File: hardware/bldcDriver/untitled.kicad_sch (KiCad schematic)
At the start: 84 parts, among them Q1 KNY3406C, Q10 KNY3406C, Q11 KNY3406C, Q12 KNY3406C, Q2 KNY3406C, Q3 KNY3406C, Q4 KNY3406C, Q5 KNY3406C, Q6 KNY3406C, Q7 KNY3406C, Q8 KNY3406C, Q9 KNY3406C, U1 FD6288Q, U4 FD6288Q

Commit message: motor sch update
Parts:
- renumbered C33 to C22, C34 to C23, C35 to C24, C31 to C25, C36 to C26, C32 to C27, C37 to C28, C23 to C29, C24 to C30, C38 to C31, C39 to C32, C22 to C33, C40 to C34, C25 to C35, C26 to C36, C41 to C37, C42 to C38, C27 to C39, C43 to C40, C28 to C41, C44 to C43, C30 to C45, Q2 to Q1, Q6 to Q10, Q1 to Q2, Q7 to Q3, Q8 to Q4, Q3 to Q5, Q4 to Q6, Q9 to Q7, Q10 to Q8, Q5 to Q9, R29 to R10, R12 to R11, R30 to R12, R8 to R13, R9 to R14, R31 to R15, R32 to R16, R7 to R17, R10 to R18, R33 to R19, R34 to R20, R14 to R21, R15 to R22, R35 to R23, R36 to R24, R16 to R25, R37 to R26, R17 to R27, R18 to R28, R38 to R29, R39 to R30, R19 to R31, R20 to R32, R40 to R33, R41 to R34, R24 to R41, R25 to R42, R45 to R43, R46 to R44, R26 to R45, R27 to R46, R11 to R7, R13 to R8, R28 to R9

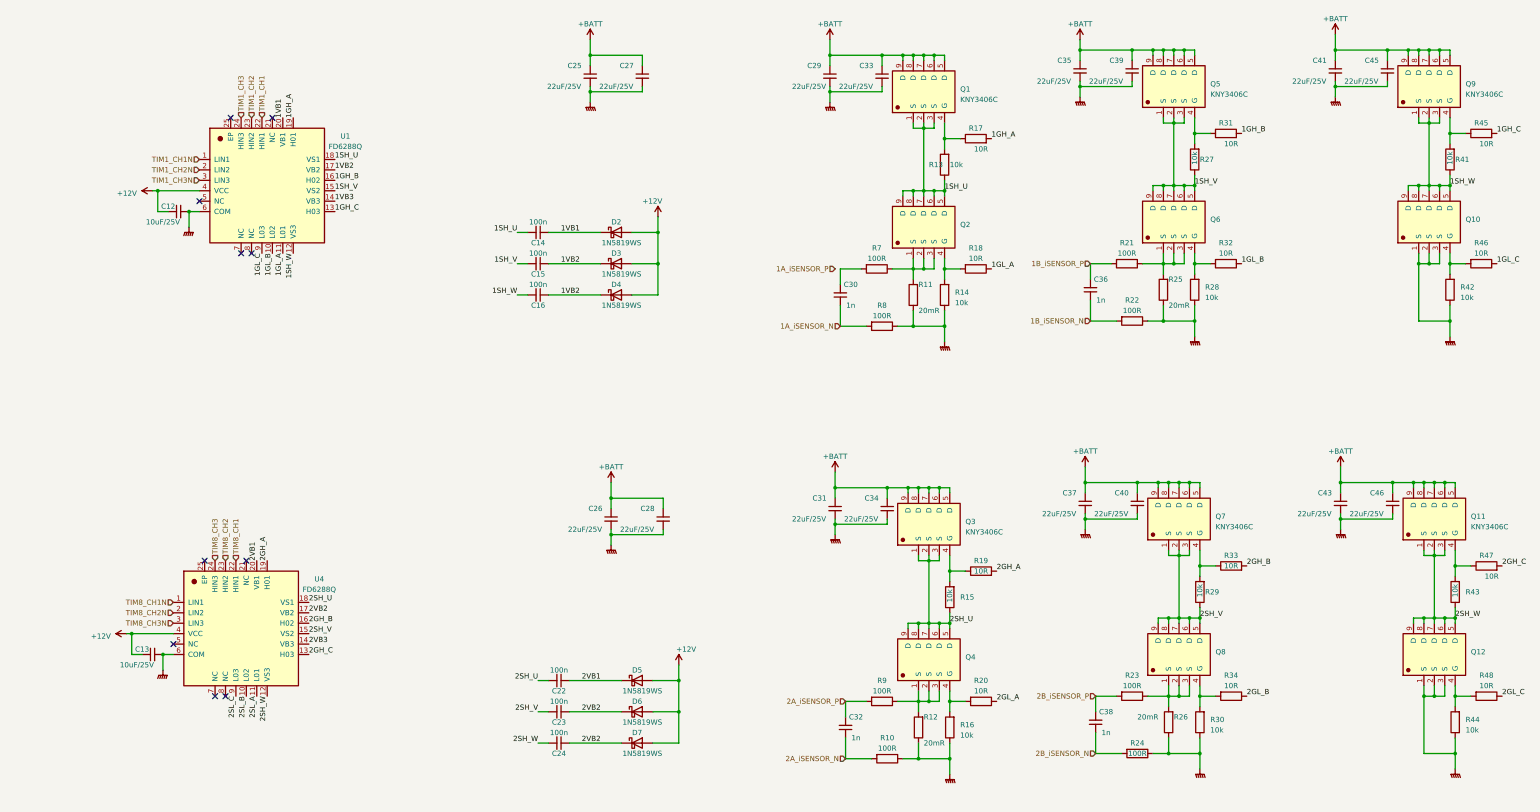
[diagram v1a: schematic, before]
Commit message: motorDriver sch update
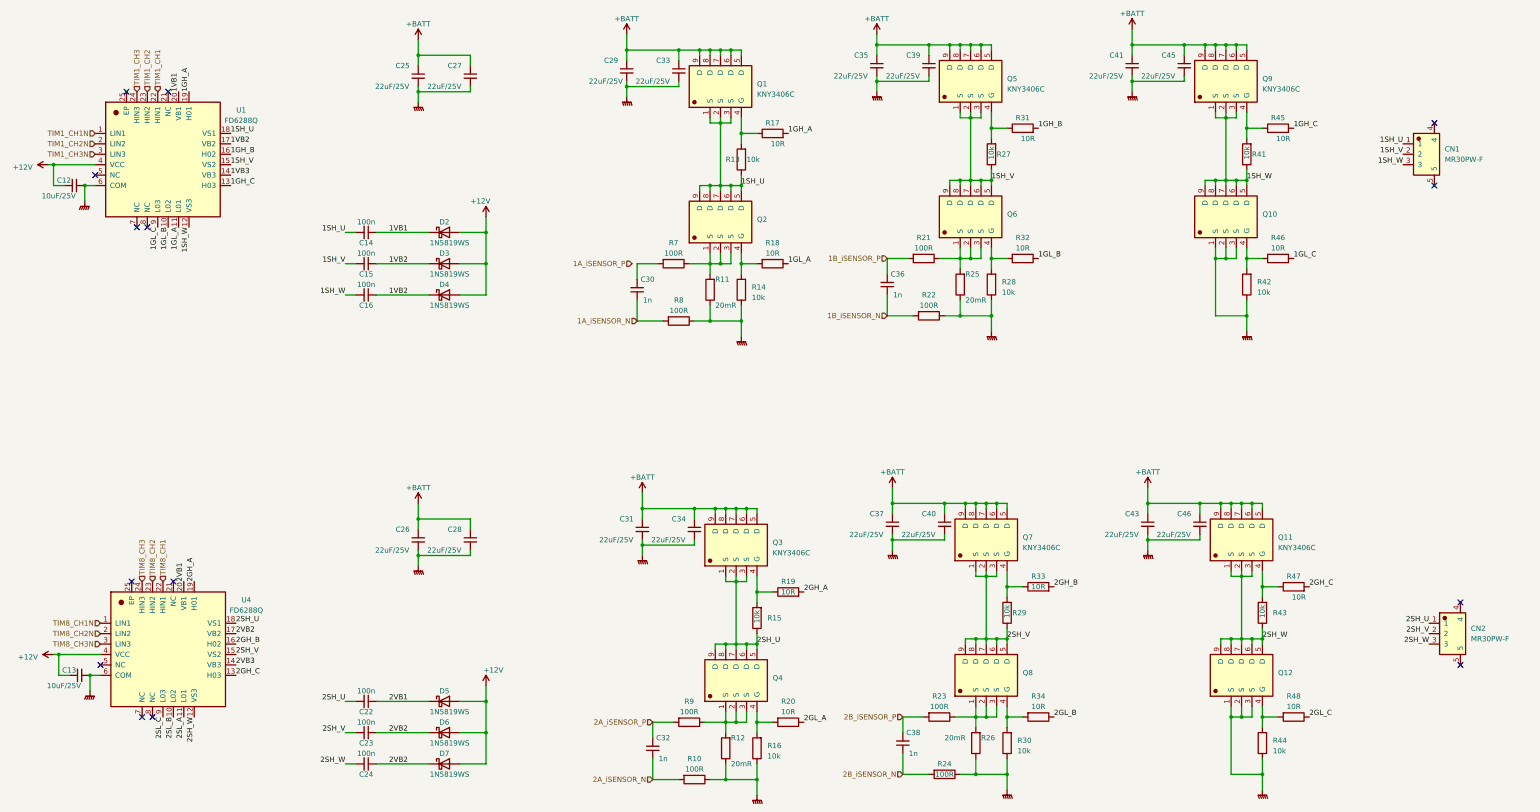
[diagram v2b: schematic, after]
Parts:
- added CN1, CN2: MR30PW-F, kicadLib:CONN-TH_MR30PW-F, symbol kicadLib:MR30PW-F
- C12, C13, C25, C26, C27, C28, C29, C31, C33, C34, C35, C37, C39, C40, C41, C43, C45, C46: footprint (none) -> Capacitor_SMD:C_0805_2012Metric_Pad1.18x1.45mm_HandSolder
- C14, C15, C16, C22, C23, C24, C30, C32, C36, C38: footprint (none) -> Capacitor_SMD:C_0603_1608Metric_Pad1.08x0.95mm_HandSolder
- Q1, Q10, Q11, Q12, Q2, Q3, Q4, Q5, Q6, Q7, Q8, Q9: footprint kicad_lceda:PDFN-8_L4.9-W5.8-P1.27-LS6.1-BL -> kicadLib:PDFN-8_L4.9-W5.8-P1.27-LS6.1-BL
- R10, R13, R14, R15, R16, R17, R18, R19, R20, R21, R22, R23, R24, R27, R28, R29, R30, R31, R32, R33, R34, R41, R42, R43, R44, R45, R46, R47, R48, R7, R8, R9: footprint (none) -> Resistor_SMD:R_0603_1608Metric_Pad0.98x0.95mm_HandSolder
- R11, R12, R25, R26: footprint (none) -> Resistor_SMD:R_2512_6332Metric_Pad1.40x3.35mm_HandSolder
- U1, U4: footprint kicad_lceda:QFN-24_L4.0-W4.0-P0.50-BL-EP2.7 -> kicadLib:QFN-24_L4.0-W4.0-P0.50-BL-EP2.6
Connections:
- net 1SH_U: now also CN1.1
- net 1SH_V: now also CN1.2
- net 1SH_W: now also CN1.3
- net 2SH_U: now also CN2.1
- net 2SH_V: now also CN2.2
- net 2SH_W: now also CN2.3
- no-connect marks 10 -> 14
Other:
- moved on the sheet: C12, C13, C14, C15, C16, C22, C23, C24, C25, C26, C27, C28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

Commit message: update motorDriver sch
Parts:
- CN1, CN2: footprint kicadLib:CONN-TH_MR30PW-F -> balancerDriver:CONN-TH_MR30PW-F
- Q1, Q10, Q11, Q12, Q2, Q3, Q4, Q5, Q6, Q7, Q8, Q9: footprint kicadLib:PDFN-8_L4.9-W5.8-P1.27-LS6.1-BL -> balancerDriver:PDFN-8_L4.9-W5.8-P1.27-LS6.1-BL
- U1, U4: footprint kicadLib:QFN-24_L4.0-W4.0-P0.50-BL-EP2.6 -> balancerDriver:QFN-24_L4.0-W4.0-P0.50-BL-EP2.6
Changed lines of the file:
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@@
 			)
 		)
-		(property "Footprint" "kicadLib:PDFN-8_L4.9-W5.8-P1.27-LS6.1-BL"
+		(property "Footprint" "balancerDriver:PDFN-8_L4.9-W5.8-P1.27-LS6.1-BL"
 			(at 312.2676 91.44 0)
 			(effects
@@
 			)
 		)
-		(property "Footprint" "kicadLib:PDFN-8_L4.9-W5.8-P1.27-LS6.1-BL"
+		(property "Footprint" "balancerDriver:PDFN-8_L4.9-W5.8-P1.27-LS6.1-BL"
 			(at 316.0776 203.2 0)
 			(effects
@@
 			)
 		)
-		(property "Footprint" "kicadLib:PDFN-8_L4.9-W5.8-P1.27-LS6.1-BL"
+		(property "Footprint" "balancerDriver:PDFN-8_L4.9-W5.8-P1.27-LS6.1-BL"
 			(at 316.0776 170.18 0)
 			(effects
@@
 			)
 		)
-		(property "Footprint" "kicadLib:CONN-TH_MR30PW-F"
+		(property "Footprint" "balancerDriver:CONN-TH_MR30PW-F"
 			(at 364.49 70.866 0)
 			(effects
@@
 			)
 		)
-		(property "Footprint" "kicadLib:PDFN-8_L4.9-W5.8-P1.27-LS6.1-BL"
+		(property "Footprint" "balancerDriver:PDFN-8_L4.9-W5.8-P1.27-LS6.1-BL"
 			(at 312.2676 58.42 0)
 			(effects
@@
 			)
 		)
-		(property "Footprint" "kicadLib:PDFN-8_L4.9-W5.8-P1.27-LS6.1-BL"
+		(property "Footprint" "balancerDriver:PDFN-8_L4.9-W5.8-P1.27-LS6.1-BL"
 			(at 189.0776 92.71 0)
 			(effects
@@
 			)
 		)
-		(property "Footprint" "kicadLib:PDFN-8_L4.9-W5.8-P1.27-LS6.1-BL"
+		(property "Footprint" "balancerDriver:PDFN-8_L4.9-W5.8-P1.27-LS6.1-BL"
 			(at 192.8876 171.45 0)
 			(effects
@@
 	)
 	(symbol
-		(lib_name "kicadLib:MR30PW-F")
 		(lib_id "kicadLib:MR30PW-F")
 		(at 370.84 193.04 0)
@@
 			)
 		)
-		(property "Footprint" "kicadLib:CONN-TH_MR30PW-F"
+		(property "Footprint" "balancerDriver:CONN-TH_MR30PW-F"
 			(at 370.84 187.706 0)
 			(effects
@@
 			)
 		)
-		(property "Footprint" "kicadLib:PDFN-8_L4.9-W5.8-P1.27-LS6.1-BL"
+		(property "Footprint" "balancerDriver:PDFN-8_L4.9-W5.8-P1.27-LS6.1-BL"
 			(at 192.8876 204.47 0)
 			(effects
@@
 			)
 		)
-		(property "Footprint" "kicadLib:PDFN-8_L4.9-W5.8-P1.27-LS6.1-BL"
+		(property "Footprint" "balancerDriver:PDFN-8_L4.9-W5.8-P1.27-LS6.1-BL"
 			(at 250.0376 58.42 0)
 			(effects
@@
 			)
 		)
-		(property "Footprint" "kicadLib:PDFN-8_L4.9-W5.8-P1.27-LS6.1-BL"
+		(property "Footprint" "balancerDriver:PDFN-8_L4.9-W5.8-P1.27-LS6.1-BL"
 			(at 253.8476 170.18 0)
 			(effects
@@
 			)
 		)
-		(property "Footprint" "kicadLib:QFN-24_L4.0-W4.0-P0.50-BL-EP2.6"
+		(property "Footprint" "balancerDriver:QFN-24_L4.0-W4.0-P0.50-BL-EP2.6"
 			(at 59.69 182.2704 0)
 			(effects
@@
 			)
 		)
-		(property "Footprint" "kicadLib:QFN-24_L4.0-W4.0-P0.50-BL-EP2.6"
+		(property "Footprint" "balancerDriver:QFN-24_L4.0-W4.0-P0.50-BL-EP2.6"
 			(at 58.42 62.8904 0)
 			(effects
@@
 			)
 		)
-		(property "Footprint" "kicadLib:PDFN-8_L4.9-W5.8-P1.27-LS6.1-BL"
+		(property "Footprint" "balancerDriver:PDFN-8_L4.9-W5.8-P1.27-LS6.1-BL"
 			(at 189.0776 59.69 0)
 			(effects
@@
 			)
 		)
-		(property "Footprint" "kicadLib:PDFN-8_L4.9-W5.8-P1.27-LS6.1-BL"
+		(property "Footprint" "balancerDriver:PDFN-8_L4.9-W5.8-P1.27-LS6.1-BL"
 			(at 253.8476 203.2 0)
 			(effects
@@
 			)
 		)
-		(property "Footprint" "kicadLib:PDFN-8_L4.9-W5.8-P1.27-LS6.1-BL"
+		(property "Footprint" "balancerDriver:PDFN-8_L4.9-W5.8-P1.27-LS6.1-BL"
 			(at 250.0376 91.44 0)
 			(effects

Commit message: update driver pcb
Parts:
- removed C13: 10uF/25V, Capacitor_SMD:C_0805_2012Metric_Pad1.18x1.45mm_HandSolder, symbol Device:C_Small
- removed C22, C23, C24: 100n, Capacitor_SMD:C_0603_1608Metric_Pad1.08x0.95mm_HandSolder, symbol Device:C_Small
- removed D5, D6, D7: 1N5819WS, Diode_SMD:D_SOD-323, symbol Diode:1N5819WS
- removed U1, U4: FD6288Q, balancerDriver:QFN-24_L4.0-W4.0-P0.50-BL-EP2.6, symbol bldcDriver:FD6288Q
- added D10, D11, D12: 1N5819WS, Diode_SMD:D_SOD-323, symbol Diode:1N5819WS
- added U1, U11: FD6288T, balancerDriver:TSSOP-20_L6.5-W4.4-P0.65-LS6.4-BL, symbol bldcDriver:FD6288T
- C12: value 10uF/25V -> 100nF/25V; footprint Capacitor_SMD:C_0805_2012Metric_Pad1.18x1.45mm_HandSolder -> Capacitor_SMD:C_0603_1608Metric_Pad1.08x0.95mm_HandSolder
- C25: value 22uF/25V -> 100nF/25V; footprint Capacitor_SMD:C_0805_2012Metric_Pad1.18x1.45mm_HandSolder -> Capacitor_SMD:C_0603_1608Metric_Pad1.08x0.95mm_HandSolder
- C26, C27, C28: value 22uF/25V -> 100n; footprint Capacitor_SMD:C_0805_2012Metric_Pad1.18x1.45mm_HandSolder -> Capacitor_SMD:C_0603_1608Metric_Pad1.08x0.95mm_HandSolder
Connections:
- net +12V: now also D10.2 (A), D11.2 (A), D12.2 (A); no longer C12.1
- net +BATT: no longer C25.1, C26.1, C27.1, C28.1
- net 1GH_A: now also U11.19 (HO1)
- net 1GH_B: now also U11.16 (HO2)
- net 1GH_C: now also U11.13 (HO3)
- net 1GL_A: now also U11.11 (LO1)
- net 1GL_B: now also U11.10 (LO2)
- net 1GL_C: now also U11.9 (LO3)
- net 1SH_U: now also C26.1, U11.18 (VS1); no longer C14.2
- net 1SH_V: now also C27.1, Q10.5 (D), Q10.6 (D), Q10.7 (D), Q10.8 (D), Q10.9 (D), Q9.1 (S), Q9.2 (S), Q9.3 (S), R41.1, U11.15 (VS2); no longer C15.2, Q5.1 (S), Q5.2 (S), Q5.3 (S), Q6.5 (D), Q6.6 (D), Q6.7 (D), Q6.8 (D), Q6.9 (D), R27.1
- net 1SH_W: now also C28.1, Q5.1 (S), Q5.2 (S), Q5.3 (S), Q6.5 (D), Q6.6 (D), Q6.7 (D), Q6.8 (D), Q6.9 (D), R27.1, U11.12 (VS3); no longer C16.2, Q10.5 (D), Q10.6 (D), Q10.7 (D), Q10.8 (D), Q10.9 (D), Q9.1 (S), Q9.2 (S), Q9.3 (S), R41.1
- net 1VB1: now also C26.2, D10.1 (K), U11.20 (VB1); no longer C14.1, D2.1 (K)
- net 1VB2: now also C27.2, D11.1 (K), U11.17 (VB2); no longer C15.1, C16.1, D3.1 (K), D4.1 (K)
- net 1VB3: now also C28.2, D12.1 (K), U11.14 (VB3)
- net 2GH_A: now also U1.19 (HO1)
- net 2GH_B: now also U1.16 (HO2)
- net 2GH_C: now also U1.13 (HO3)
- net 2GL_A: now also U1.11 (LO1)
- net 2GL_B: now also U1.10 (LO2)
- net 2GL_C: now also U1.9 (LO3)
- net 2SH_U: now also C14.1, U1.18 (VS1)
- net 2SH_V: now also C15.1, Q11.1 (S), Q11.2 (S), Q11.3 (S), Q12.5 (D), Q12.6 (D), Q12.7 (D), Q12.8 (D), Q12.9 (D), R43.1, U1.15 (VS2); no longer Q7.1 (S), Q7.2 (S), Q7.3 (S), Q8.5 (D), Q8.6 (D), Q8.7 (D), Q8.8 (D), Q8.9 (D), R29.1
- net 2SH_W: now also C16.1, Q7.1 (S), Q7.2 (S), Q7.3 (S), Q8.5 (D), Q8.6 (D), Q8.7 (D), Q8.8 (D), Q8.9 (D), R29.1, U1.12 (VS3); no longer Q11.1 (S), Q11.2 (S), Q11.3 (S), Q12.5 (D), Q12.6 (D), Q12.7 (D), Q12.8 (D), Q12.9 (D), R43.1
- net 2VB1: now also C14.2, D2.1 (K), U1.20 (VB1)
- net 2VB2: now also C15.2, D3.1 (K), U1.17 (VB2)
- net 2VB3: now also C16.2, D4.1 (K), U1.14 (VB3)
- net GNDPWR: now also C12.1, C25.1, U1.8 (COM), U11.8 (COM); no longer C12.2, C25.2, C26.2, C27.2, C28.2
- net TIM1_CH1: now also U11.1 (HIN1)
- net TIM1_CH1N: now also U11.4 (LIN1)
- net TIM1_CH2: now also U11.2 (HIN2)
- net TIM1_CH2N: now also U11.5 (LIN2)
- net TIM1_CH3: now also U11.3 (HIN3)
- net TIM1_CH3N: now also U11.6 (LIN3)
- net TIM8_CH1: now also U1.4 (LIN1)
- net TIM8_CH1N: now also U1.1 (HIN1)
- net TIM8_CH2: now also U1.5 (LIN2)
- net TIM8_CH2N: now also U1.2 (HIN2)
- net TIM8_CH3: now also U1.6 (LIN3)
- net TIM8_CH3N: now also U1.3 (HIN3)
- new net: C25.2, U11.7 (VCC)
- new net: C12.2, U1.7 (VCC)
- no-connect marks 14 -> 4
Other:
- moved on the sheet: C29, C30, C31, C32, C33, C34, C35, C36, C37, C38, C39, C40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

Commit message: update pcbs
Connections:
- net 2SH_U: now also CN2.3; no longer CN2.1
- net 2SH_W: now also CN2.1; no longer CN2.3
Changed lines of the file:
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@@
-		)
-	)
-	(label "2SH_W"
-		(at 382.27 195.58 180)
-		(fields_autoplaced yes)
-		(effects
-			(font
-				(size 1.27 1.27)
-			)
-			(justify right bottom)
 		)
 	)
@@
 	)
 	(label "2SH_U"
-		(at 382.27 190.5 180)
-		(fields_autoplaced yes)
-		(effects
-			(font
-				(size 1.27 1.27)
-			)
-			(justify right bottom)
-		)
-	)
-	(label "2SH_U"
 		(at 85.09 191.77 0)
 		(fields_autoplaced yes)
@@
 		)
 	)
+	(label "2SH_W"
+		(at 382.27 190.5 180)
+		(fields_autoplaced yes)
+		(effects
+			(font
+				(size 1.27 1.27)
+			)
+			(justify right bottom)
+		)
+	)
 	(label "1GH_C"
 		(at 81.28 91.44 0)
@@
 		)
 	)
+	(label "2SH_U"
+		(at 382.27 195.58 180)
+		(fields_autoplaced yes)
+		(effects
+			(font
+				(size 1.27 1.27)
+			)
+			(justify right bottom)
+		)
+	)

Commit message: motorDriver pcb update
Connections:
- net 1A_iSENSOR_P: now also C30.2, R7.2
- net 1B_iSENSOR_N renamed 1B_iSENSOR-
- net 1B_iSENSOR_P renamed 1B_iSENSOR+
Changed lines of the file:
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@@
 		)
 	)
-	(hierarchical_label "1B_iSENSOR_N"
+	(hierarchical_label "1B_iSENSOR-"
 		(shape input)
 		(at 257.81 114.3 180)
@@
 		)
 	)
-	(hierarchical_label "1B_iSENSOR_P"
+	(hierarchical_label "1B_iSENSOR+"
 		(shape input)
 		(at 257.81 100.33 180)
@@
 	(hierarchical_label "1A_iSENSOR_P"
 		(shape input)
-		(at 190.5 100.33 180)
+		(at 191.77 100.33 180)
 		(fields_autoplaced yes)
 		(effects

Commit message: update motorDriver pcb
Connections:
- net 1A_iSENSOR_N renamed 1A_ISENSOR-
- net 1A_iSENSOR_P renamed 1A_ISENSOR+
- net 1B_iSENSOR+ renamed 1B_ISENSOR+
- net 1B_iSENSOR- renamed 1B_ISENSOR-
- net 2A_iSENSOR_N renamed 2A_ISENSOR-
- net 2A_iSENSOR_P renamed 2A_ISENSOR+
- net 2B_iSENSOR_N renamed 2B_ISENSOR-
- net 2B_iSENSOR_P renamed 2B_ISENSOR+
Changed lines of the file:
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@@
 		)
 	)
-	(hierarchical_label "1B_iSENSOR-"
+	(hierarchical_label "1B_ISENSOR-"
 		(shape input)
 		(at 257.81 114.3 180)
@@
 		)
 	)
-	(hierarchical_label "1A_iSENSOR_N"
+	(hierarchical_label "1A_ISENSOR-"
 		(shape input)
 		(at 191.77 114.3 180)
@@
 		)
 	)
-	(hierarchical_label "2B_iSENSOR_N"
+	(hierarchical_label "2B_ISENSOR-"
 		(shape input)
 		(at 254 227.33 180)
@@
 		)
 	)
-	(hierarchical_label "1B_iSENSOR+"
+	(hierarchical_label "1B_ISENSOR+"
 		(shape input)
 		(at 257.81 100.33 180)
@@
 		)
 	)
-	(hierarchical_label "2A_iSENSOR_N"
+	(hierarchical_label "2A_ISENSOR-"
 		(shape input)
 		(at 187.96 224.79 180)
@@
 		)
 	)
-	(hierarchical_label "2B_iSENSOR_P"
+	(hierarchical_label "2B_ISENSOR+"
 		(shape input)
 		(at 254 213.36 180)
@@
 		)
 	)
-	(hierarchical_label "2A_iSENSOR_P"
+	(hierarchical_label "2A_ISENSOR+"
 		(shape input)
 		(at 187.96 210.82 180)
@@
 		)
 	)
-	(hierarchical_label "1A_iSENSOR_P"
+	(hierarchical_label "1A_ISENSOR+"
 		(shape input)
 		(at 191.77 100.33 180)

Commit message: update driver pcn
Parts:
- C29, C31, C33, C34, C35, C37, C39, C40, C41, C43, C45, C46: footprint Capacitor_SMD:C_0805_2012Metric_Pad1.18x1.45mm_HandSolder -> Capacitor_SMD:C_1206_3216Metric_Pad1.33x1.80mm_HandSolder
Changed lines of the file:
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@@
 			)
 		)
-		(property "Footprint" "Capacitor_SMD:C_0805_2012Metric_Pad1.18x1.45mm_HandSolder"
+		(property "Footprint" "Capacitor_SMD:C_1206_3216Metric_Pad1.33x1.80mm_HandSolder"
 			(at 326.39 166.37 0)
 			(effects
@@
 			)
 		)
-		(property "Footprint" "Capacitor_SMD:C_0805_2012Metric_Pad1.18x1.45mm_HandSolder"
+		(property "Footprint" "Capacitor_SMD:C_1206_3216Metric_Pad1.33x1.80mm_HandSolder"
 			(at 189.23 53.34 0)
 			(effects
@@
 			)
 		)
-		(property "Footprint" "Capacitor_SMD:C_0805_2012Metric_Pad1.18x1.45mm_HandSolder"
+		(property "Footprint" "Capacitor_SMD:C_1206_3216Metric_Pad1.33x1.80mm_HandSolder"
 			(at 313.69 166.37 0)
 			(effects
@@
 			)
 		)
-		(property "Footprint" "Capacitor_SMD:C_0805_2012Metric_Pad1.18x1.45mm_HandSolder"
+		(property "Footprint" "Capacitor_SMD:C_1206_3216Metric_Pad1.33x1.80mm_HandSolder"
 			(at 198.12 163.83 0)
 			(effects
@@
 			)
 		)
-		(property "Footprint" "Capacitor_SMD:C_0805_2012Metric_Pad1.18x1.45mm_HandSolder"
+		(property "Footprint" "Capacitor_SMD:C_1206_3216Metric_Pad1.33x1.80mm_HandSolder"
 			(at 267.97 53.34 0)
 			(effects
@@
 			)
 		)
-		(property "Footprint" "Capacitor_SMD:C_0805_2012Metric_Pad1.18x1.45mm_HandSolder"
+		(property "Footprint" "Capacitor_SMD:C_1206_3216Metric_Pad1.33x1.80mm_HandSolder"
 			(at 251.46 166.37 0)
 			(effects
@@
 			)
 		)
-		(property "Footprint" "Capacitor_SMD:C_0805_2012Metric_Pad1.18x1.45mm_HandSolder"
+		(property "Footprint" "Capacitor_SMD:C_1206_3216Metric_Pad1.33x1.80mm_HandSolder"
 			(at 330.2 53.34 0)
 			(effects
@@
 			)
 		)
-		(property "Footprint" "Capacitor_SMD:C_0805_2012Metric_Pad1.18x1.45mm_HandSolder"
+		(property "Footprint" "Capacitor_SMD:C_1206_3216Metric_Pad1.33x1.80mm_HandSolder"
 			(at 185.42 163.83 0)
 			(effects
@@
 			)
 		)
-		(property "Footprint" "Capacitor_SMD:C_0805_2012Metric_Pad1.18x1.45mm_HandSolder"
+		(property "Footprint" "Capacitor_SMD:C_1206_3216Metric_Pad1.33x1.80mm_HandSolder"
 			(at 264.16 166.37 0)
 			(effects
@@
 			)
 		)
-		(property "Footprint" "Capacitor_SMD:C_0805_2012Metric_Pad1.18x1.45mm_HandSolder"
+		(property "Footprint" "Capacitor_SMD:C_1206_3216Metric_Pad1.33x1.80mm_HandSolder"
 			(at 255.27 53.34 0)
 			(effects
@@
 			)
 		)
-		(property "Footprint" "Capacitor_SMD:C_0805_2012Metric_Pad1.18x1.45mm_HandSolder"
+		(property "Footprint" "Capacitor_SMD:C_1206_3216Metric_Pad1.33x1.80mm_HandSolder"
 			(at 317.5 53.34 0)
 			(effects
@@
 			)
 		)
-		(property "Footprint" "Capacitor_SMD:C_0805_2012Metric_Pad1.18x1.45mm_HandSolder"
+		(property "Footprint" "Capacitor_SMD:C_1206_3216Metric_Pad1.33x1.80mm_HandSolder"
 			(at 201.93 53.34 0)
 			(effects
